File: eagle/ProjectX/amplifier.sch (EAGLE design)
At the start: 8 parts, among them U1 TC4427COA, U2 TC4427COA

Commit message: Some work on the final design
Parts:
- removed C3: 4.7uF, rcl:C-EUC0805
- removed C4: 100nF, rcl:C-EUC0805
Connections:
- net GND: now also U1.NC, U2.NC; no longer C3.2, C4.2
- net VCC: now also U1.NC_2, U2.NC_2; no longer C3.1, C4.1
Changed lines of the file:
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@@
 <?xml version="1.0" encoding="utf-8"?>
 <!DOCTYPE eagle SYSTEM "eagle.dtd">
-<eagle version="8.3.2">
+<eagle version="8.4.1">
 <drawing>
 <settings>
@@
 <part name="P+5" library="supply1" library_urn="urn:adsk.eagle:library:371" deviceset="VCC" device=""/>
 <part name="U2" library="Microchip_By_element14_Batch_1" deviceset="TC4427COA" device=""/>
-<part name="C3" library="rcl" library_urn="urn:adsk.eagle:library:334" deviceset="C-EU" device="C0805" package3d_urn="urn:adsk.eagle:package:23617/2" value="4.7uF"/>
-<part name="C4" library="rcl" library_urn="urn:adsk.eagle:library:334" deviceset="C-EU" device="C0805" package3d_urn="urn:adsk.eagle:package:23617/2" value="100nF"/>
 <part name="P+6" library="supply1" library_urn="urn:adsk.eagle:library:371" deviceset="VCC" device=""/>
 <part name="GND6" library="supply1" library_urn="urn:adsk.eagle:library:371" deviceset="GND" device=""/>
+<part name="GND7" library="supply1" library_urn="urn:adsk.eagle:library:371" deviceset="GND" device=""/>
+<part name="P+7" library="supply1" library_urn="urn:adsk.eagle:library:371" deviceset="VCC" device=""/>
+<part name="P+8" library="supply1" library_urn="urn:adsk.eagle:library:371" deviceset="VCC" device=""/>
+<part name="GND8" library="supply1" library_urn="urn:adsk.eagle:library:371" deviceset="GND" device=""/>
 </parts>
 <sheets>
@@
 <instance part="P+5" gate="VCC" x="55.88" y="111.76"/>
 <instance part="U2" gate="A" x="10.16" y="43.18" rot="R270"/>
-<instance part="C3" gate="G$1" x="-12.7" y="66.04"/>
-<instance part="C4" gate="G$1" x="-5.08" y="66.04"/>
 <instance part="P+6" gate="VCC" x="5.08" y="73.66"/>
-<instance part="GND6" gate="1" x="-12.7" y="55.88"/>
+<instance part="GND6" gate="1" x="2.54" y="66.04" rot="R180"/>
+<instance part="GND7" gate="1" x="5.08" y="20.32"/>
+<instance part="P+7" gate="VCC" x="-38.1" y="20.32" rot="R90"/>
+<instance part="P+8" gate="VCC" x="-2.54" y="22.86" rot="R90"/>
+<instance part="GND8" gate="1" x="-30.48" y="20.32"/>
 </instances>
 <busses>
@@
 <pinref part="U2" gate="A" pin="VDD"/>
 <pinref part="P+6" gate="VCC" pin="VCC"/>
-<wire x1="5.08" y1="60.96" x2="5.08" y2="68.58" width="0.1524" layer="91"/>
-<pinref part="C4" gate="G$1" pin="1"/>
-<wire x1="5.08" y1="68.58" x2="5.08" y2="71.12" width="0.1524" layer="91"/>
-<wire x1="5.08" y1="68.58" x2="-5.08" y2="68.58" width="0.1524" layer="91"/>
-<junction x="5.08" y="68.58"/>
-<pinref part="C3" gate="G$1" pin="1"/>
-<wire x1="-5.08" y1="68.58" x2="-12.7" y2="68.58" width="0.1524" layer="91"/>
-<junction x="-5.08" y="68.58"/>
+<wire x1="5.08" y1="60.96" x2="5.08" y2="71.12" width="0.1524" layer="91"/>
+</segment>
+<segment>
+<pinref part="P+8" gate="VCC" pin="VCC"/>
+<pinref part="U2" gate="A" pin="NC_2"/>
+<wire x1="0" y1="22.86" x2="2.54" y2="22.86" width="0.1524" layer="91"/>
+<wire x1="2.54" y1="22.86" x2="2.54" y2="25.4" width="0.1524" layer="91"/>
+</segment>
+<segment>
+<pinref part="P+7" gate="VCC" pin="VCC"/>
+<pinref part="U1" gate="A" pin="NC_2"/>
+<wire x1="-35.56" y1="20.32" x2="-33.02" y2="20.32" width="0.1524" layer="91"/>
+<wire x1="-33.02" y1="20.32" x2="-33.02" y2="25.4" width="0.1524" layer="91"/>
 </segment>
 </net>
@@
 <segment>
 <pinref part="U2" gate="A" pin="GND"/>
-<pinref part="C4" gate="G$1" pin="2"/>
-<wire x1="2.54" y1="60.96" x2="-5.08" y2="60.96" width="0.1524" layer="91"/>
-<pinref part="C3" gate="G$1" pin="2"/>
-<wire x1="-5.08" y1="60.96" x2="-12.7" y2="60.96" width="0.1524" layer="91"/>
-<junction x="-5.08" y="60.96"/>
+<wire x1="2.54" y1="60.96" x2="2.54" y2="63.5" width="0.1524" layer="91"/>
 <pinref part="GND6" gate="1" pin="GND"/>
-<wire x1="-12.7" y1="58.42" x2="-12.7" y2="60.96" width="0.1524" layer="91"/>
-<junction x="-12.7" y="60.96"/>
+</segment>
+<segment>
+<pinref part="U2" gate="A" pin="NC"/>
+<pinref part="GND7" gate="1" pin="GND"/>
+<wire x1="5.08" y1="25.4" x2="5.08" y2="22.86" width="0.1524" layer="91"/>
+</segment>
+<segment>
+<pinref part="U1" gate="A" pin="NC"/>
+<pinref part="GND8" gate="1" pin="GND"/>
+<wire x1="-30.48" y1="25.4" x2="-30.48" y2="22.86" width="0.1524" layer="91"/>
 </segment>
 </net>
@@
 <net name="N$5" class="0">
 <segment>
-<wire x1="-25.4" y1="76.2" x2="-25.4" y2="60.96" width="0.1524" layer="91"/>
+<wire x1="-25.4" y1="78.74" x2="-25.4" y2="60.96" width="0.1524" layer="91"/>
 <pinref part="U1" gate="A" pin="IN_A"/>
 <pinref part="SV2" gate="1" pin="40"/>
-<wire x1="-25.4" y1="76.2" x2="2.54" y2="76.2" width="0.1524" layer="91"/>
-<wire x1="2.54" y1="76.2" x2="10.16" y2="83.82" width="0.1524" layer="91"/>
+<wire x1="-25.4" y1="78.74" x2="0" y2="81.28" width="0.1524" layer="91"/>
+<wire x1="0" y1="81.28" x2="10.16" y2="83.82" width="0.1524" layer="91"/>
 </segment>
 </net>
@@
 <pinref part="SV1" gate="1" pin="33"/>
 <pinref part="U2" gate="A" pin="*OUT_B"/>
-<wire x1="20.32" y1="15.24" x2="17.78" y2="15.24" width="0.1524" layer="91"/>
-<wire x1="17.78" y1="15.24" x2="7.62" y2="25.4" width="0.1524" layer="91"/>
+<wire x1="20.32" y1="15.24" x2="20.32" y2="17.78" width="0.1524" layer="91"/>
+<wire x1="20.32" y1="17.78" x2="7.62" y2="25.4" width="0.1524" layer="91"/>
 </segment>
 </net>
@@
 <pinref part="U1" gate="A" pin="*OUT_A"/>
 <pinref part="SV1" gate="1" pin="39"/>
-<wire x1="-25.4" y1="25.4" x2="2.54" y2="25.4" width="0.1524" layer="91"/>
-<wire x1="2.54" y1="25.4" x2="12.7" y2="15.24" width="0.1524" layer="91"/>
+<wire x1="-25.4" y1="25.4" x2="-7.62" y2="17.78" width="0.1524" layer="91"/>
+<wire x1="-7.62" y1="17.78" x2="12.7" y2="15.24" width="0.1524" layer="91"/>
 </segment>
 </net>
@@
 <pinref part="U1" gate="A" pin="*OUT_B"/>
 <pinref part="SV1" gate="1" pin="37"/>
-<wire x1="-27.94" y1="25.4" x2="5.08" y2="25.4" width="0.1524" layer="91"/>
-<wire x1="5.08" y1="25.4" x2="15.24" y2="15.24" width="0.1524" layer="91"/>
-</segment>
-</net>
+<wire x1="-27.94" y1="25.4" x2="-10.16" y2="20.32" width="0.1524" layer="91"/>
+<wire x1="-10.16" y1="20.32" x2="15.24" y2="15.24" width="0.1524" layer="91"/>
+</segment>
+</net>

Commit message: More work on the 32 bit board
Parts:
- added C10, C12, C18, C20, C26, C28, C6: 100nF, rcl:C-EUC0805
- added C11, C17, C19, C25, C27, C5, C9: 4.7uF, rcl:C-EUC0805
- added U10, U11, U12, U17, U18, U19, U20, U25, U26, U27, U28, U5, U6, U9: TC4427COA, Microchip_By_element14_Batch_1:TC4427COA
- SV1, SV2: device con-lstb:MA20-2W -> Parts:MA20-2W
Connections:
- new net N$10: SV1.1, U2.*OUT_A
- new net N$100: SV1.25, U26.*OUT_A
- new net N$101: SV1.26, U26.*OUT_B
- new net N$102: SV2.25, U26.IN_A
- new net N$103: SV1.27, U25.*OUT_A
- new net N$104: SV1.28, U25.*OUT_B
- new net N$105: SV2.30, U27.IN_B
- new net N$106: SV2.29, U27.IN_A
- new net N$107: SV2.32, U28.IN_B
- new net N$108: SV1.31, U28.*OUT_A
- new net N$109: SV1.32, U28.*OUT_B
- new net N$11: SV1.3, U1.*OUT_A
- new net N$110: SV2.31, U28.IN_A
- new net N$111: SV1.29, U27.*OUT_A
- new net N$112: SV1.30, U27.*OUT_B
- new net N$12: SV1.7, U6.*OUT_A
- new net N$13: SV1.10, U10.*OUT_B
- new net N$14: SV1.9, U10.*OUT_A
- new net N$15: SV1.11, U9.*OUT_A
- new net N$16: SV1.23, U20.*OUT_A
- new net N$17: SV2.6, U5.IN_B
- new net N$18: SV2.5, U5.IN_A
- new net N$19: SV2.8, U6.IN_B
- new net N$22: SV2.7, U6.IN_A
- new net N$23: SV1.5, U5.*OUT_A
- new net N$24: SV1.6, U5.*OUT_B
- new net N$26: SV1.15, U12.*OUT_A
- new net N$29: SV1.12, U9.*OUT_B
- new net N$33: SV2.12, U9.IN_B
- new net N$34: SV2.11, U9.IN_A
- new net N$35: SV2.10, U10.IN_B
- new net N$38: SV2.9, U10.IN_A
- new net N$41: SV2.14, U11.IN_B
- new net N$42: SV2.13, U11.IN_A
- new net N$43: SV2.16, U12.IN_B
- new net N$46: SV2.15, U12.IN_A
- new net N$47: SV1.13, U11.*OUT_A
- new net N$48: SV1.14, U11.*OUT_B
- new net N$65: SV2.20, U17.IN_B
- new net N$66: SV2.19, U17.IN_A
- new net N$67: SV2.18, U18.IN_B
- new net N$68: SV1.17, U18.*OUT_A
- new net N$69: SV1.18, U18.*OUT_B
- new net N$70: SV2.17, U18.IN_A
- new net N$71: SV1.19, U17.*OUT_A
- new net N$72: SV1.20, U17.*OUT_B
- new net N$73: SV2.22, U19.IN_B
- new net N$74: SV2.21, U19.IN_A
- new net N$75: SV2.24, U20.IN_B
- new net N$78: SV2.23, U20.IN_A
- new net N$79: SV1.21, U19.*OUT_A
- new net N$80: SV1.22, U19.*OUT_B
- new net N$9: SV1.8, U6.*OUT_B
- new net N$97: SV2.28, U25.IN_B
- new net N$98: SV2.27, U25.IN_A
- new net N$99: SV2.26, U26.IN_B
- net GND: now also C10.2, C11.2, C12.2, C17.2, C18.2, C19.2, C20.2, C25.2, C26.2, C27.2, C28.2, C5.2, C6.2, C9.2, U10.GND, U10.NC, U11.GND, U11.NC, U12.GND, U12.NC, U17.GND, U17.NC, U18.GND, U18.NC, U19.GND, U19.NC, U20.GND, U20.NC, U25.GND, U25.NC, U26.GND, U26.NC, U27.GND, U27.NC, U28.GND, U28.NC, U5.GND, U5.NC, U6.GND, U6.NC, U9.GND, U9.NC; no longer SV1.1, SV1.2, SV2.1, SV2.2
- net N$1: now also SV2.2; no longer SV2.34
- net N$2: now also SV1.2, U2.*OUT_B; no longer SV1.39, U1.*OUT_A
- net N$3: now also SV1.4; no longer SV1.37
- net N$4: now also SV2.4; no longer SV2.38
- net N$5: now also SV2.3; no longer SV2.40
- net N$6: now also SV2.1; no longer SV2.36
- net N$7: now also SV1.16, U12.*OUT_B; no longer SV1.35, U2.*OUT_A
- net N$8: now also SV1.24, U20.*OUT_B; no longer SV1.33, U2.*OUT_B
- net VCC: now also C10.1, C11.1, C12.1, C17.1, C18.1, C19.1, C20.1, C25.1, C26.1, C27.1, C28.1, C5.1, C6.1, C9.1, U10.NC_2, U10.VDD, U11.NC_2, U11.VDD, U12.NC_2, U12.VDD, U17.NC_2, U17.VDD, U18.NC_2, U18.VDD, U19.NC_2, U19.VDD, U20.NC_2, U20.VDD, U25.NC_2, U25.VDD, U26.NC_2, U26.VDD, U27.NC_2, U27.VDD, U28.NC_2, U28.VDD, U5.NC_2, U5.VDD, U6.NC_2, U6.VDD, U9.NC_2, U9.VDD; no longer SV1.3, SV1.4, SV2.3, SV2.4
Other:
- moved on the sheet: C1, C2, U2

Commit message: Added a finished board
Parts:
- added D1: (no value), SparkFun-LED:LED0603
- added J1, J2: (no value), SparkFun-Connectors:CONN_02PTH3
- added R1: 1k, SparkFun-Resistors:0.22OHM-0805-1/4W-1%
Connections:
- removed net VCC: C1.1, C10.1, C11.1, C12.1, C17.1, C18.1, C19.1, C2.1, C20.1, C25.1, C26.1, C27.1, C28.1, C5.1, C6.1, C9.1, U1.NC_2, U1.VDD, U10.NC_2, U10.VDD, U11.NC_2, U11.VDD, U12.NC_2, U12.VDD, U17.NC_2, U17.VDD, U18.NC_2, U18.VDD, U19.NC_2, U19.VDD, U2.NC_2, U2.VDD, U20.NC_2, U20.VDD, U25.NC_2, U25.VDD, U26.NC_2, U26.VDD, U27.NC_2, U27.VDD, U28.NC_2, U28.VDD, U5.NC_2, U5.VDD, U6.NC_2, U6.VDD, U9.NC_2, U9.VDD
- new net N$20: D1.A, R1.1
- new net VDD: C1.1, C10.1, C11.1, C12.1, C17.1, C18.1, C19.1, C2.1, C20.1, C25.1, C26.1, C27.1, C28.1, C5.1, C6.1, C9.1, J1.1, J2.1, R1.2, U1.NC_2, U1.VDD, U10.NC_2, U10.VDD, U11.NC_2, U11.VDD, U12.NC_2, U12.VDD, U17.NC_2, U17.VDD, U18.NC_2, U18.VDD, U19.NC_2, U19.VDD, U2.NC_2, U2.VDD, U20.NC_2, U20.VDD, U25.NC_2, U25.VDD, U26.NC_2, U26.VDD, U27.NC_2, U27.VDD, U28.NC_2, U28.VDD, U5.NC_2, U5.VDD, U6.NC_2, U6.VDD, U9.NC_2, U9.VDD
- net GND: now also D1.C, J1.2, J2.2, SV1.P$1, SV2.P$1

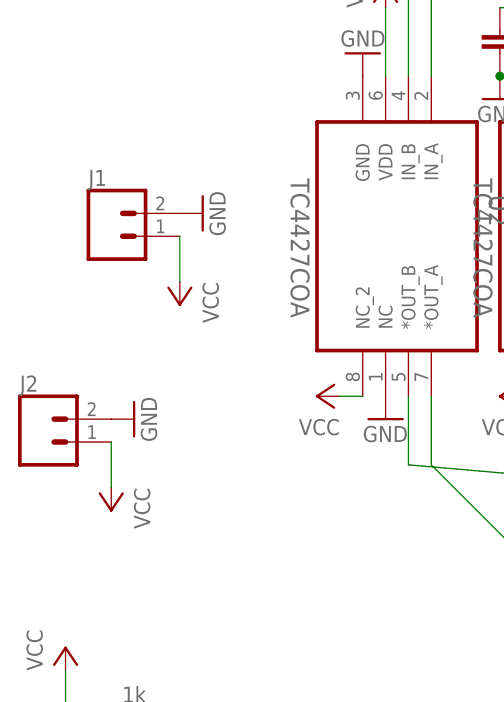
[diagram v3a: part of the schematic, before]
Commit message: Finished the small amplifier board
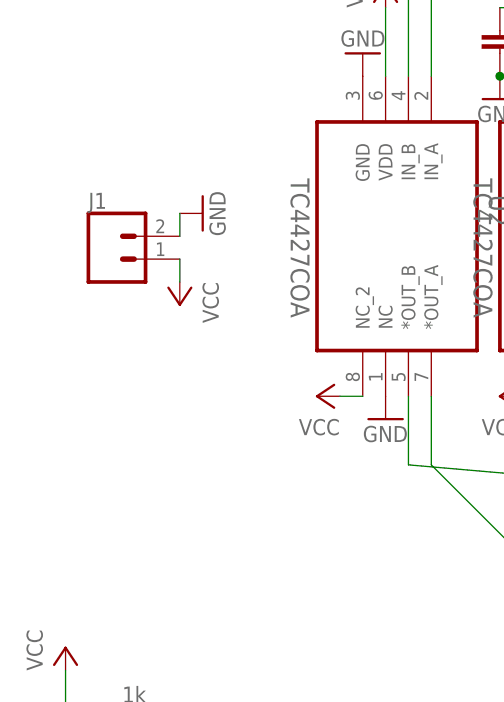
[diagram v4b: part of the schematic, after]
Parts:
- removed J2: (no value), SparkFun-Connectors:CONN_02PTH3
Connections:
- net GND: no longer J2.2
- net VDD: no longer J2.1
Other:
- moved on the sheet: J1
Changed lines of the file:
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@@
 <part name="P+32" library="supply1" library_urn="urn:adsk.eagle:library:371" deviceset="VCC" device=""/>
 <part name="J1" library="SparkFun-Connectors" library_urn="urn:adsk.eagle:library:513" deviceset="CONN_02" device="PTH3" package3d_urn="urn:adsk.eagle:package:38048/1"/>
-<part name="J2" library="SparkFun-Connectors" library_urn="urn:adsk.eagle:library:513" deviceset="CONN_02" device="PTH3" package3d_urn="urn:adsk.eagle:package:38048/1"/>
-<part name="GND19" library="supply1" library_urn="urn:adsk.eagle:library:371" deviceset="GND" device=""/>
 <part name="GND20" library="supply1" library_urn="urn:adsk.eagle:library:371" deviceset="GND" device=""/>
-<part name="P+33" library="supply1" library_urn="urn:adsk.eagle:library:371" deviceset="VCC" device=""/>
 <part name="P+34" library="supply1" library_urn="urn:adsk.eagle:library:371" deviceset="VCC" device=""/>
 <part name="D1" library="SparkFun-LED" library_urn="urn:adsk.eagle:library:529" deviceset="LED" device="0603" package3d_urn="urn:adsk.eagle:package:39354/1"/>
@@
 <instance part="P+31" gate="VCC" x="30.48" y="71.12"/>
 <instance part="P+32" gate="VCC" x="71.12" y="71.12"/>
-<instance part="J1" gate="G$1" x="-81.28" y="43.18"/>
-<instance part="J2" gate="G$1" x="-88.9" y="20.32"/>
-<instance part="GND19" gate="1" x="-78.74" y="22.86" rot="R90"/>
+<instance part="J1" gate="G$1" x="-81.28" y="40.64"/>
 <instance part="GND20" gate="1" x="-71.12" y="45.72" rot="R90"/>
-<instance part="P+33" gate="VCC" x="-81.28" y="12.7" rot="R180"/>
 <instance part="P+34" gate="VCC" x="-73.66" y="35.56" rot="R180"/>
 <instance part="D1" gate="G$1" x="-68.58" y="-10.16" rot="R90"/>
@@
 </segment>
 <segment>
-<pinref part="J2" gate="G$1" pin="1"/>
-<pinref part="P+33" gate="VCC" pin="VCC"/>
-<wire x1="-81.28" y1="15.24" x2="-81.28" y2="20.32" width="0.1524" layer="91"/>
-</segment>
-<segment>
 <pinref part="J1" gate="G$1" pin="1"/>
 <pinref part="P+34" gate="VCC" pin="VCC"/>
-<wire x1="-73.66" y1="38.1" x2="-73.66" y2="43.18" width="0.1524" layer="91"/>
+<wire x1="-73.66" y1="38.1" x2="-73.66" y2="40.64" width="0.1524" layer="91"/>
 </segment>
 <segment>
@@
 </segment>
 <segment>
-<pinref part="J2" gate="G$1" pin="2"/>
-<pinref part="GND19" gate="1" pin="GND"/>
-</segment>
-<segment>
 <pinref part="J1" gate="G$1" pin="2"/>
 <pinref part="GND20" gate="1" pin="GND"/>
-</segment>
-<segment>
+<wire x1="-73.66" y1="43.18" x2="-73.66" y2="45.72" width="0.1524" layer="91"/>
+</segment>
+<segment>
